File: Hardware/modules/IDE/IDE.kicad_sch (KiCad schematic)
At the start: 17 parts, among them J1 Conn_02x20_Odd_Even, J2 IDE_VCC, J3 Conn_02x22_Odd_Even, J4 Bus_PCI_6502, U1 74AHC1G00, U2 6525, U3 74HCT04, U4 74HC138

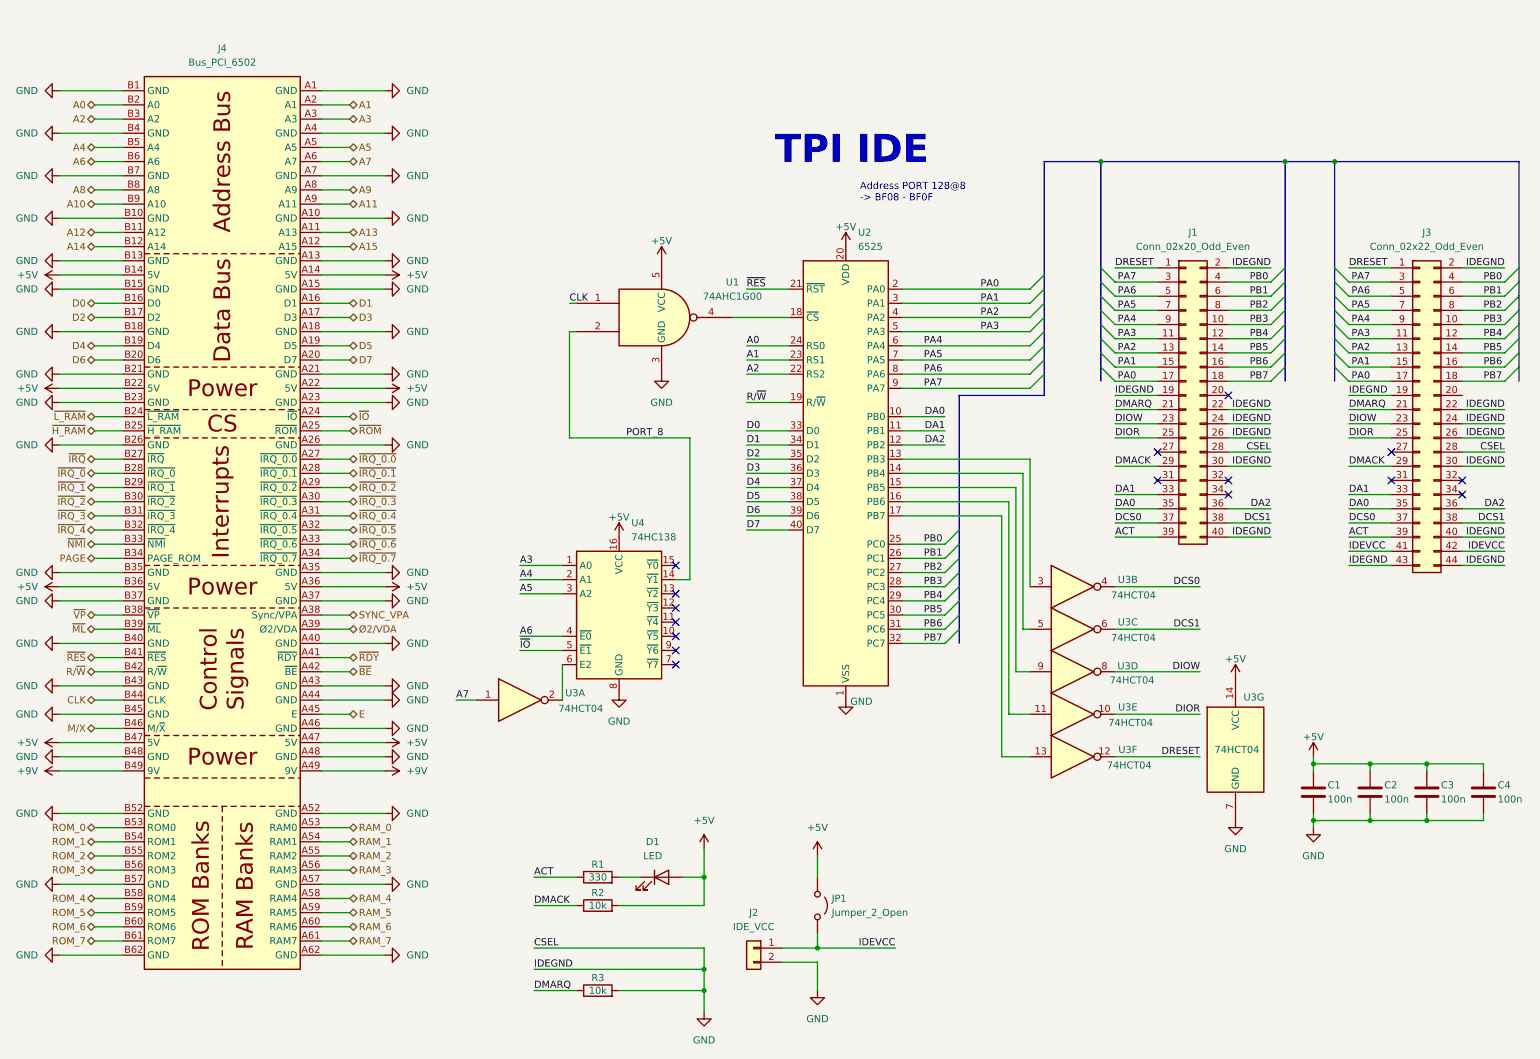
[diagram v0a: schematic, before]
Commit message: Hardware Update Add MyCPU VGA Module Beautify all Schematics minor Error corrections Readme Update
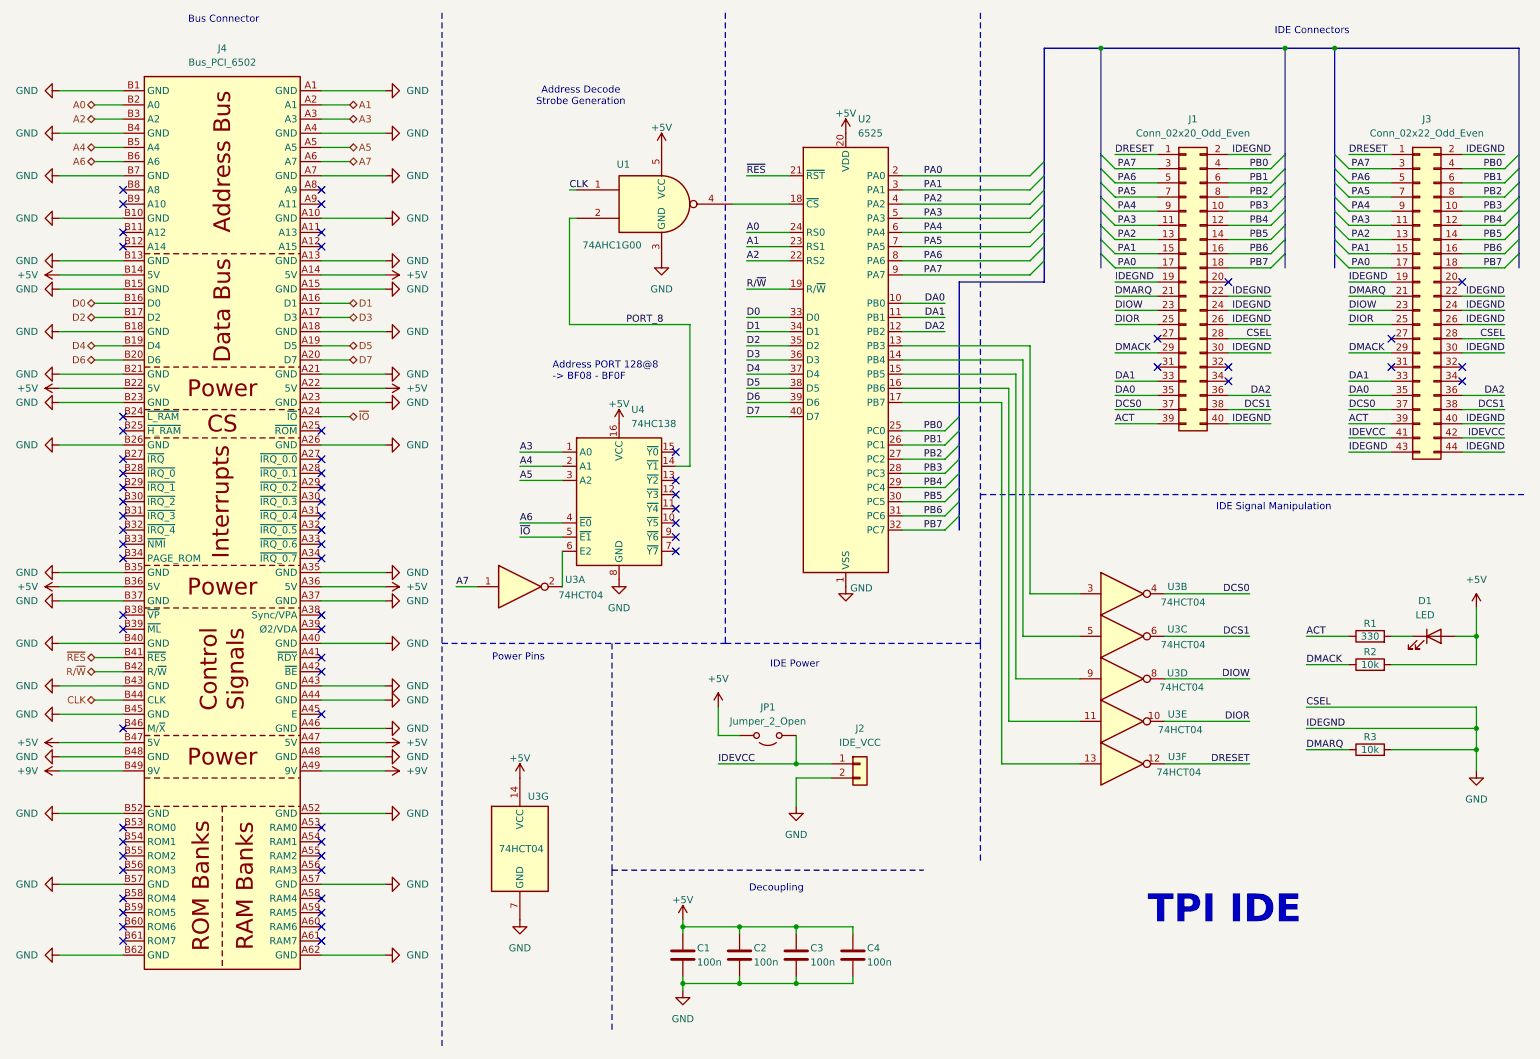
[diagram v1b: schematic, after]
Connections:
- net A10: no longer names the net of J4.B9 (A10)
- net A11: no longer names the net of J4.A9 (A11)
- net A12: no longer names the net of J4.B11 (A12)
- net A13: no longer names the net of J4.A11 (A13)
- net A14: no longer names the net of J4.B12 (A14)
- net A15: no longer names the net of J4.A12 (A15)
- net A8: no longer names the net of J4.B8 (A8)
- net A9: no longer names the net of J4.A8 (A9)
- net E: no longer names the net of J4.A45 (E)
- net M/X: no longer names the net of J4.B46 (M/~{X})
- net PAGE: no longer names the net of J4.B34 (PAGE_ROM)
- net RAM_0: no longer names the net of J4.A53 (RAM0)
- net RAM_1: no longer names the net of J4.A54 (RAM1)
- net RAM_2: no longer names the net of J4.A55 (RAM2)
- net RAM_3: no longer names the net of J4.A56 (RAM3)
- net RAM_4: no longer names the net of J4.A58 (RAM4)
- net RAM_5: no longer names the net of J4.A59 (RAM5)
- net RAM_6: no longer names the net of J4.A60 (RAM6)
- net RAM_7: no longer names the net of J4.A61 (RAM7)
- net ROM_0: no longer names the net of J4.B53 (ROM0)
- net ROM_1: no longer names the net of J4.B54 (ROM1)
- net ROM_2: no longer names the net of J4.B55 (ROM2)
- net ROM_3: no longer names the net of J4.B56 (ROM3)
- net ROM_4: no longer names the net of J4.B58 (ROM4)
- net ROM_5: no longer names the net of J4.B59 (ROM5)
- net ROM_6: no longer names the net of J4.B60 (ROM6)
- net ROM_7: no longer names the net of J4.B61 (ROM7)
- net SYNC_VPA: no longer names the net of J4.A38 (Sync/VPA)
- net ~{BE}: no longer names the net of J4.A42 (~{BE})
- net ~{H_RAM}: no longer names the net of J4.B25 (~{H_RAM})
- net ~{IRQ_0.0}: no longer names the net of J4.A27 (~{IRQ_0.0})
- net ~{IRQ_0.1}: no longer names the net of J4.A28 (~{IRQ_0.1})
- net ~{IRQ_0.2}: no longer names the net of J4.A29 (~{IRQ_0.2})
- net ~{IRQ_0.3}: no longer names the net of J4.A30 (~{IRQ_0.3})
- net ~{IRQ_0.4}: no longer names the net of J4.A31 (~{IRQ_0.4})
- net ~{IRQ_0.5}: no longer names the net of J4.A32 (~{IRQ_0.5})
- net ~{IRQ_0.6}: no longer names the net of J4.A33 (~{IRQ_0.6})
- net ~{IRQ_0.7}: no longer names the net of J4.A34 (~{IRQ_0.7})
- net ~{IRQ_0}: no longer names the net of J4.B28 (~{IRQ_0})
- net ~{IRQ_1}: no longer names the net of J4.B29 (~{IRQ_1})
- net ~{IRQ_2}: no longer names the net of J4.B30 (~{IRQ_2})
- net ~{IRQ_3}: no longer names the net of J4.B31 (~{IRQ_3})
- net ~{IRQ_4}: no longer names the net of J4.B32 (~{IRQ_4})
- net ~{IRQ}: no longer names the net of J4.B27 (~{IRQ})
- net ~{L_RAM}: no longer names the net of J4.B24 (~{L_RAM})
- net ~{ML}: no longer names the net of J4.B39 (~{ML})
- net ~{NMI}: no longer names the net of J4.B33 (~{NMI})
- net ~{RDY}: no longer names the net of J4.A41 (~{RDY})
- net ~{ROM}: no longer names the net of J4.A25 (~{ROM})
- net ~{VP}: no longer names the net of J4.B38 (~{VP})
- net Ø2/VDA: no longer names the net of J4.A39 (Ø2/VDA)
- no-connect marks 16 -> 68
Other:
- note added: "Address Decode Strobe Generation"
- note added: "Bus Connector"
- note added: "Decoupling"
- note added: "IDE Connectors"
- note added: "IDE Power"
- note added: "IDE Signal Manipulation"
- note added: "Power Pins"
- company: (none) -> Synthron
- title: (none) -> S65xx Computer System
- moved on the sheet: C1, C2, C3, C4, D1, J1, J2, J3, JP1, R1, R2, R3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

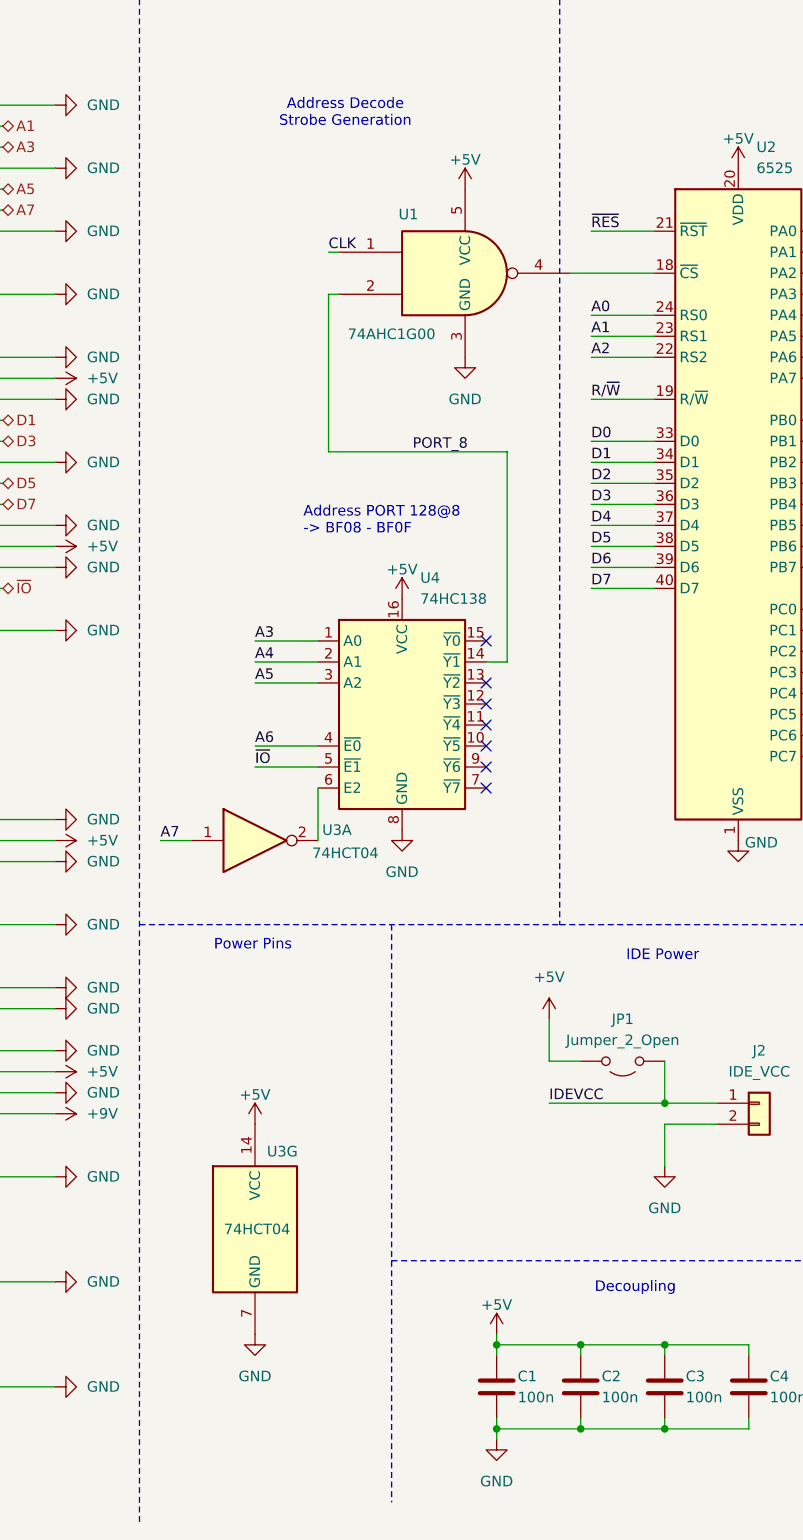
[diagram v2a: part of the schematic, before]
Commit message: Chip Select Strobe Generation Bugfix
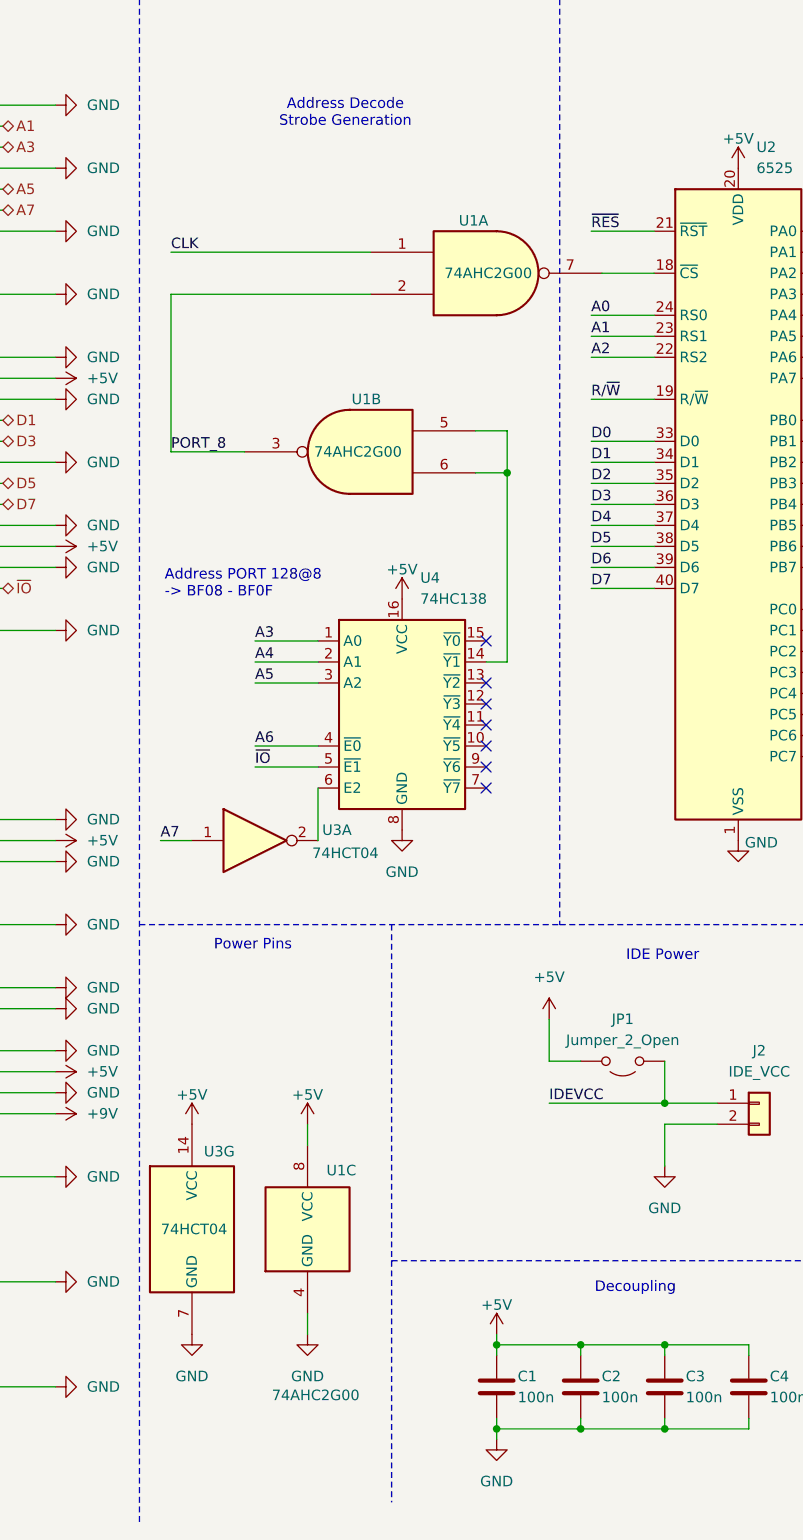
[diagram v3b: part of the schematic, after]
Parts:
- removed U1: 74AHC1G00, Package_TO_SOT_SMD:SOT-23-5_HandSoldering, symbol 74xGxx:74AHC1G00
- added U1: 74AHC2G00, Package_SO:TSSOP-8_3x3mm_P0.65mm, symbol 74xGxx:74AHC2G00
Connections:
- net +5V: now also U1.8 (VCC)
- net CLK: now also U1.1
- net GND: now also U1.4 (GND)
- net PORT_8: now also U1.2, U1.3; no longer U4.14 (~{Y1})
- net at U2.18 (~{CS}): now also U1.7
- new net: U1.5, U1.6, U4.14 (~{Y1})
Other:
- moved on the sheet: U3G

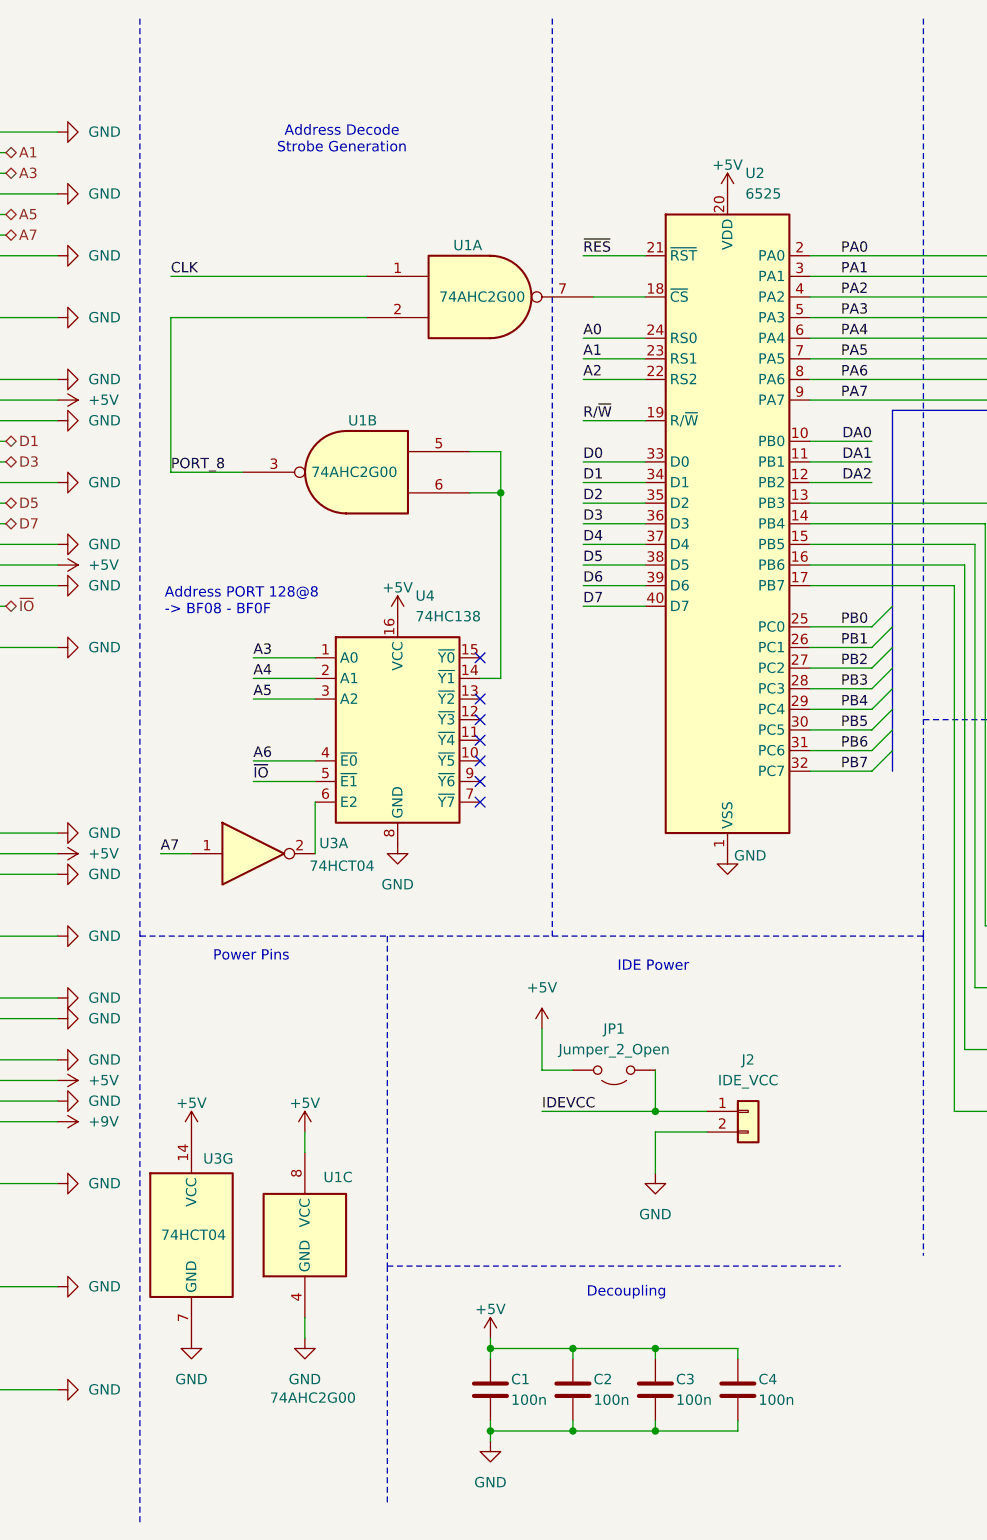
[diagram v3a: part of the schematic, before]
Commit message: Hardware Review Pt. 1 fix Address Decoding for Strobe Generators add bulk capacitance to every board fix wiring of Prototyping Board
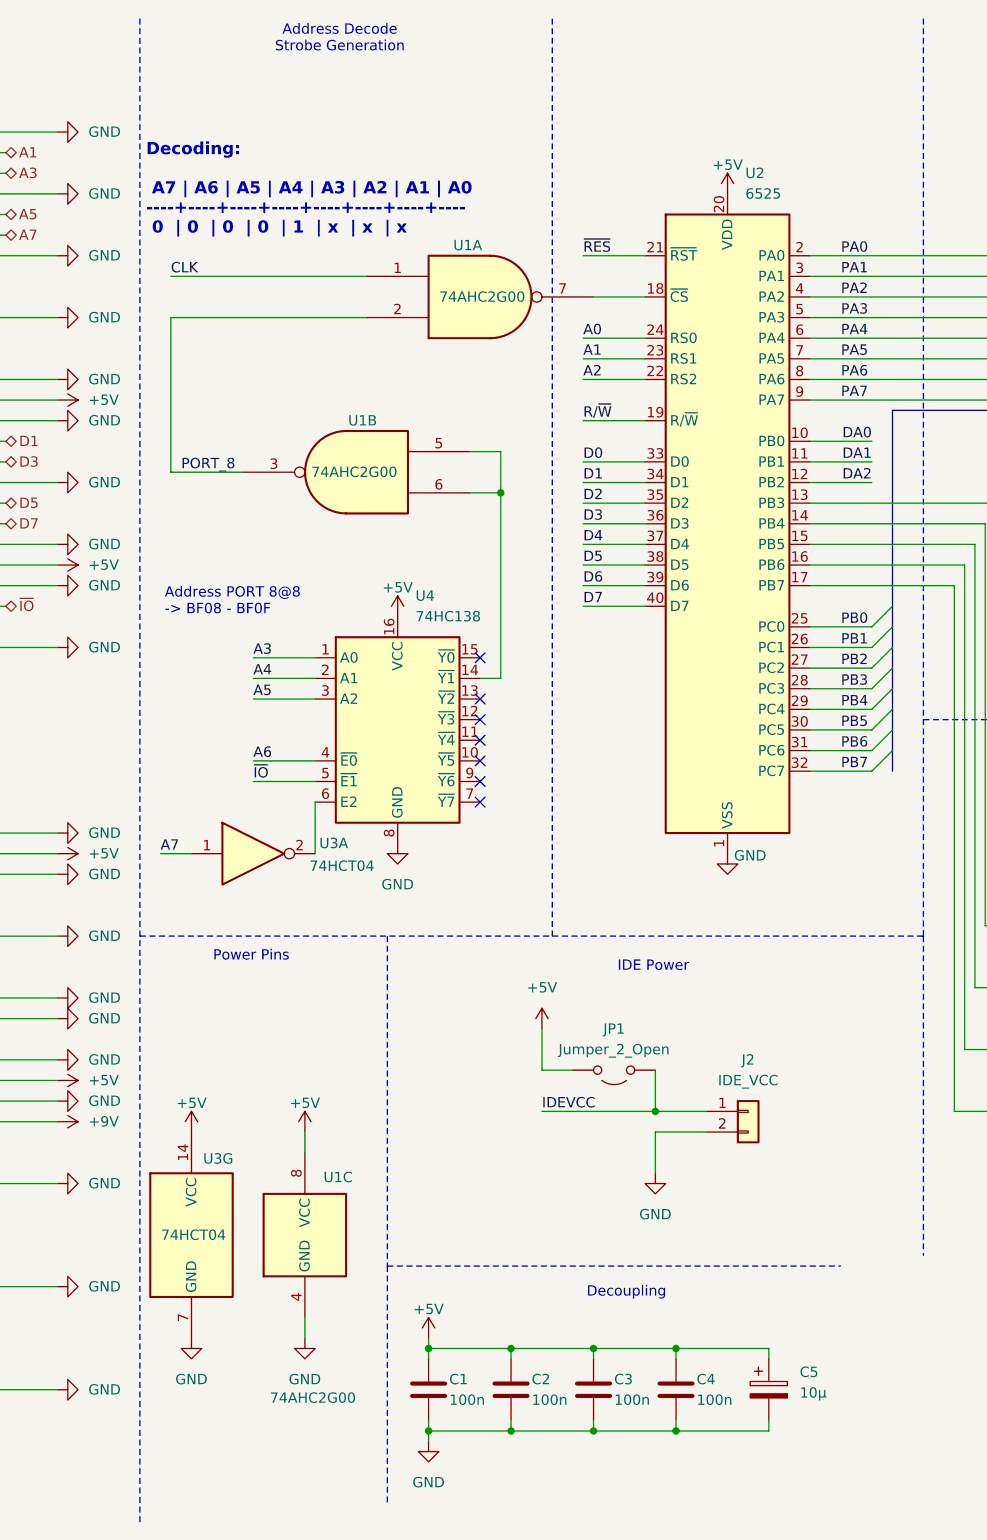
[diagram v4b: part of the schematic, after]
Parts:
- added C5: 10µ, Capacitor_THT:CP_Radial_D5.0mm_P2.50mm, symbol Device:C_Polarized
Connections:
- net +5V: now also C5.1
- net GND: now also C5.2
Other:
- note added: "Address PORT 8@8 -> BF08 - BF0F"
- note added: "Decoding: A7 | A6 | A5 | A4 | A3 | A2 | A1 | A0 ----+----+----+----+----+----+----+---- 0 | 0 | 0 | 0 | 1 | x | x | x"
- note removed: "Address PORT 128@8 -> BF08 - BF0F"
- moved on the sheet: C1, C2, C3, C4
